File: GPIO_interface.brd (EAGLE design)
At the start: 38 x 34.5 mm, 33 parts

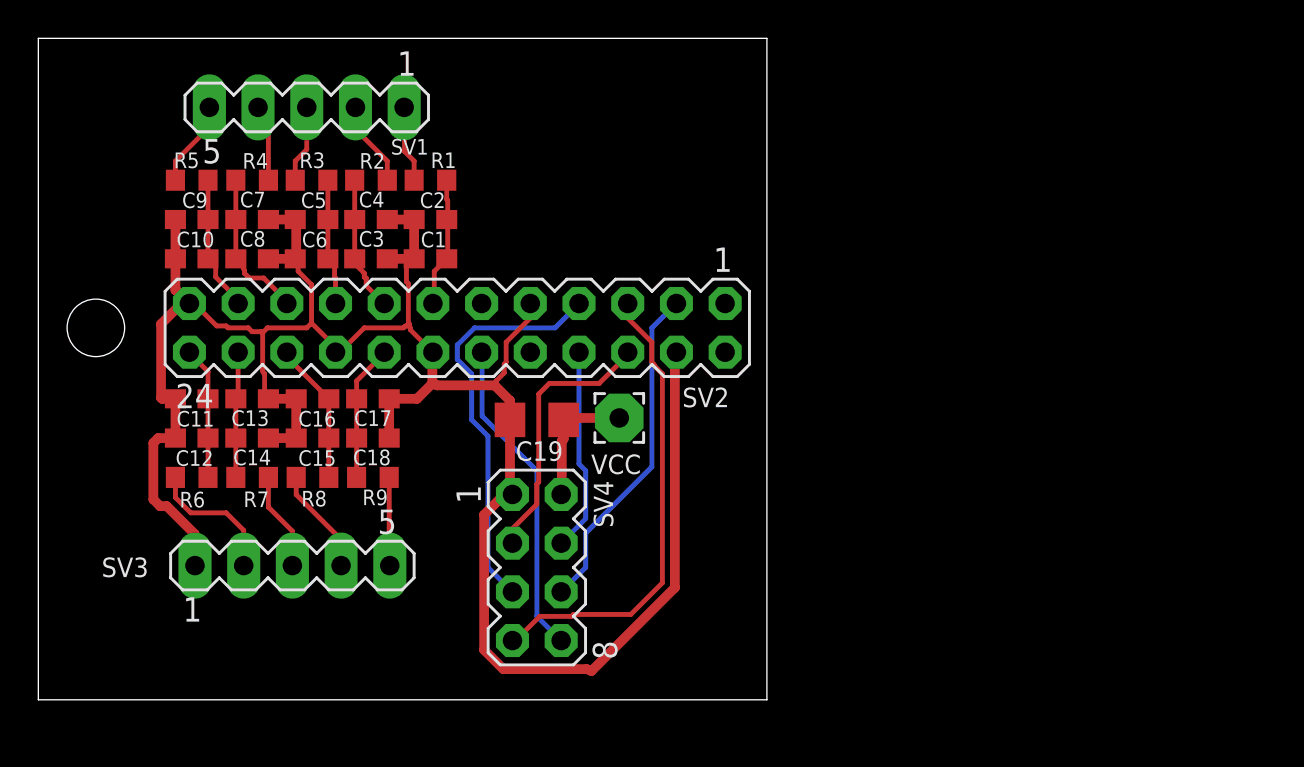
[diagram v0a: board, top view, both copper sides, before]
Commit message: wersja pod pcbs.io
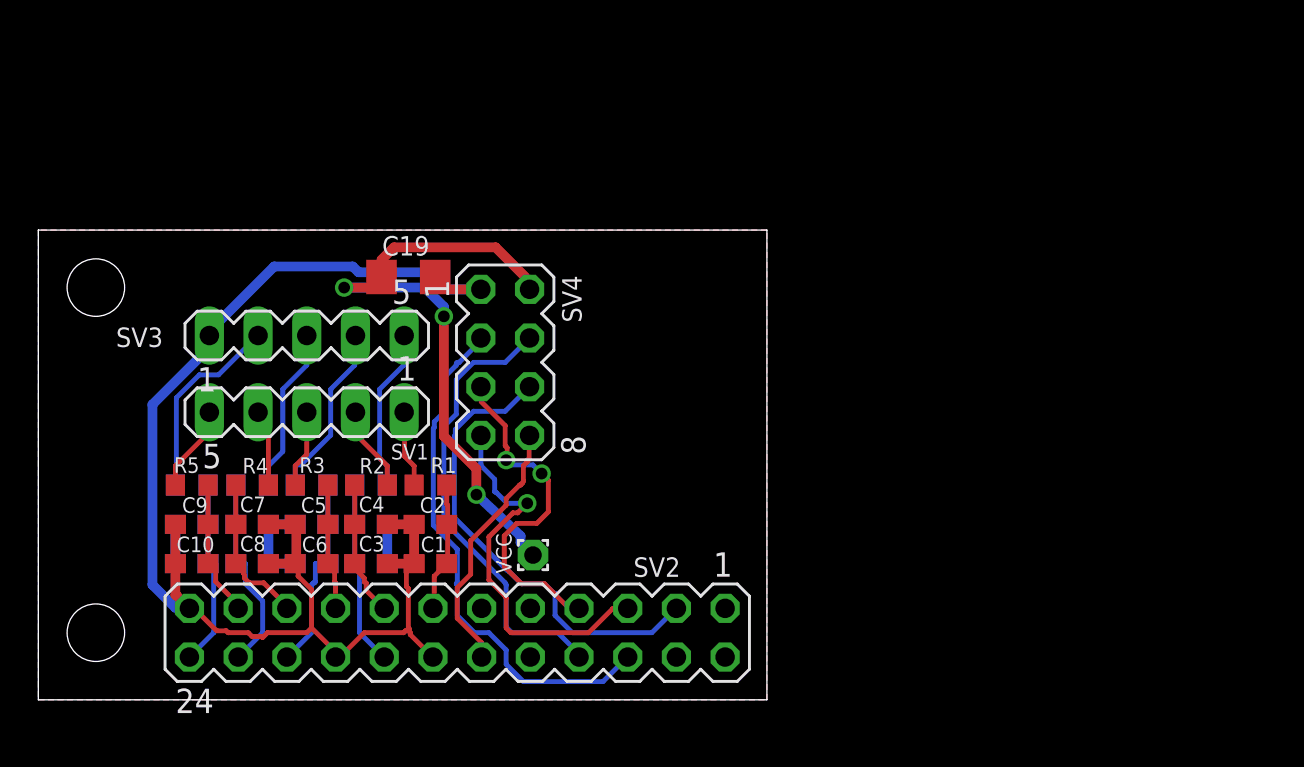
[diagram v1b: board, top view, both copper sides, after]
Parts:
- VCC: device wirepad:2,54/1,0 -> wirepad:1,6/0,9
- moved R1 15.9 mm to (20.4, 10.7)
- moved R2 15.9 mm to (17.4, 10.7)
- moved R3 15.9 mm to (14.2, 10.7)
- moved R4 15.9 mm to (11.2, 10.7)
- moved R5 15.9 mm to (8.00, 10.7)
- moved C1 15.9 mm to (20.4, 6.60)
- moved C10 15.9 mm to (8.00, 6.60)
- moved C2 15.9 mm to (20.4, 8.65)
- moved C3 15.9 mm to (17.4, 6.60)
- moved C4 15.9 mm to (17.4, 8.65)
- moved C5 15.9 mm to (14.2, 8.65)
- moved C6 15.9 mm to (14.2, 6.60)
- moved C7 15.9 mm to (11.2, 8.65)
- moved C8 15.9 mm to (11.2, 6.60)
- moved C9 15.9 mm to (8.00, 8.65)
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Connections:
- net GND: no longer SV2.4, SV2.9
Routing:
- net GND: track 117.4 -> 82.0 mm
- net VCC: track 6.94 -> 32.8 mm, vias 0 -> 3
- net CE: track 14.0 -> 27.4 mm
- net CSN: track 10.6 -> 23.8 mm
- net MOSI: track 17.5 -> 24.7 mm
- net MISO: track 24.4 -> 20.0 mm, vias 0 -> 1
- net IN9: track 4.61 -> 8.51 mm
- net IN8: track 5.57 -> 9.27 mm
- net OUT7: track 6.76 -> 10.4 mm
- net IN7: track 5.12 -> 8.63 mm
- net SCK: track 21.3 -> 17.9 mm, vias 0 -> 2
- net IN6: track 7.16 -> 10.2 mm
- net OUT6: track 6.93 -> 9.80 mm
- net IRQ: track 16.8 -> 13.9 mm
- net OUT8: track 7.44 -> 10.3 mm
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- added copper zone on layer 1, net GND
- added copper zone on layer 16, net GND
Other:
- board size 38 x 34.5 mm -> 38 x 24.5 mm

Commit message: add LDO, use whole RPI connector
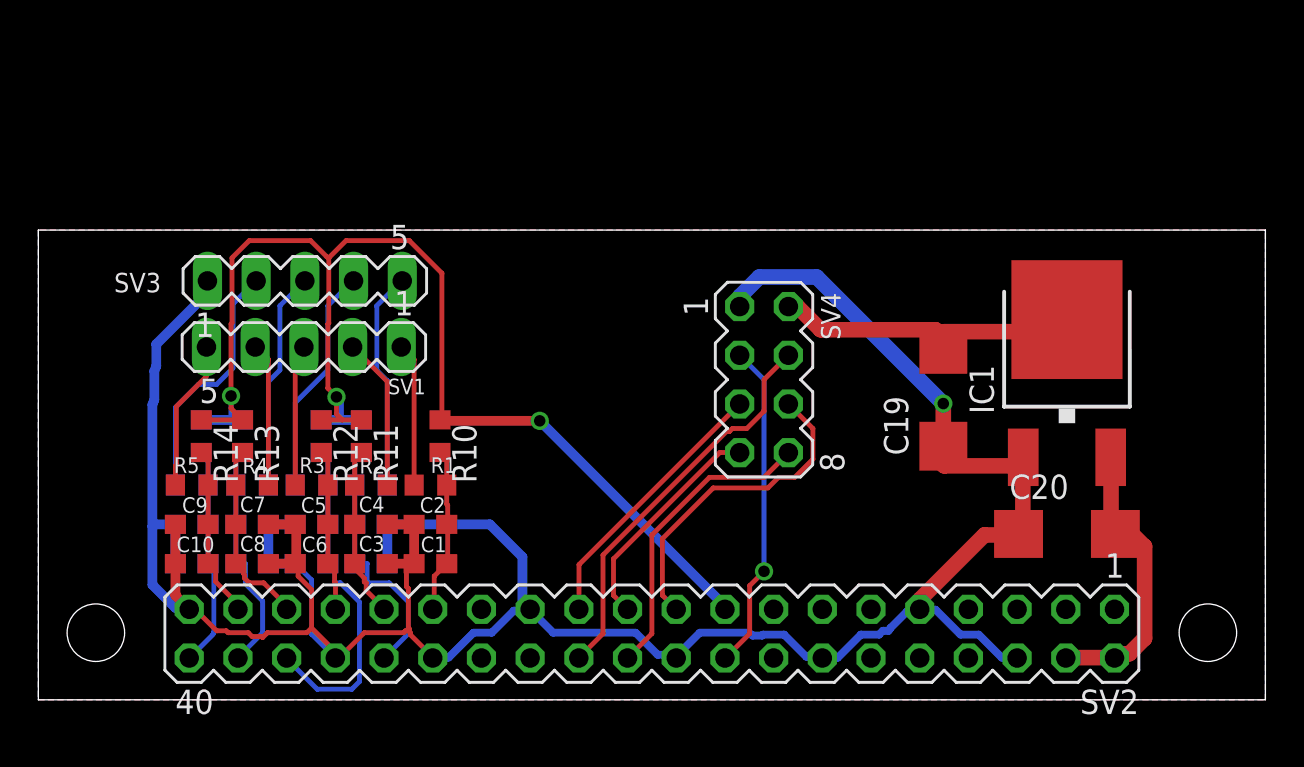
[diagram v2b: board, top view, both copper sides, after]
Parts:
- removed VCC: 3.3V, wirepad:1,6/0,9
- added C20: 10u, rcl:C/6032-28R
- added IC1: LD117ADT33TR, v-reg:DPACK
- added R10, R11, R12, R13, R14, R15, R16, R17, R18: 270, rcl:R0603
- C19: device rcl:C1206 -> rcl:C/6032-28R
- SV2: device con-lstb:MA12-2 -> con-lstb:MA20-2
- moved C19 28.6 mm to (47.2, 15.2), turned to 90 degrees
- moved SV4 13.5 mm to (37.9, 16.2)
- moved SV2 10.2 mm to (32.0, 2.95)
- moved SV1 3.40 mm to (13.8, 17.9)
- moved SV3 2.85 mm to (13.9, 21.4)
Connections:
- removed net CE: SV2.6, SV4.3
- new net N$1: C20.+, IC1.3, SV2.2, SV2.4
- new net N$2: C19.+, IC1.4, SV4.2
- new net RST: SV2.18, SV4.3
- net CSN: now also SV2.24; no longer SV2.8
- net GND: now also C19.-, C20.-, IC1.1, SV2.20, SV2.25, SV2.30, SV2.34, SV2.39, SV2.6, SV2.9; no longer C19.2, SV2.18, SV2.23
- net IRQ: now also SV2.22; no longer SV2.12
- net MISO: now also SV2.21; no longer SV2.5
- net MOSI: now also SV2.19; no longer SV2.3
- net OUT1: now also R10.2, SV2.29; no longer SV2.13
- net OUT2: now also R11.2, SV2.31; no longer SV2.15
- net OUT3: now also R12.2, SV2.33; no longer SV2.17
- net OUT4: now also R13.2, SV2.35; no longer SV2.19
- net OUT5: now also R14.2, SV2.37; no longer SV2.21
- net OUT6: now also R15.2, SV2.40; no longer SV2.24
- net OUT7: now also R16.2, SV2.38; no longer SV2.22
- net OUT8: now also R17.2, SV2.36; no longer SV2.20
- net OUT9: now also R18.2, SV2.32; no longer SV2.16
- net SCK: now also SV2.23; no longer SV2.7
- net VCC: now also R10.1, R11.1, R12.1, R13.1, R14.1, R15.1, R16.1, R17.1, R18.1, SV2.17; no longer C19.1, SV4.2, VCC.1
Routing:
- net GND: track 82.0 -> 152.8 mm, vias 0 -> 1
- net VCC: track 32.8 -> 69.8 mm
- net CE: track 27.4 -> 0.00 mm
- net N$2: track 0.00 -> 17.3 mm
- net RST: track 0.00 -> 17.2 mm, vias 0 -> 1
- net N$1: track 0.00 -> 15.2 mm
- net MISO: track 20.0 -> 11.8 mm, vias 1 -> 0
- net OUT8: track 10.3 -> 18.0 mm
- net MOSI: track 24.7 -> 17.0 mm
- net OUT9: track 9.76 -> 13.8 mm
- net SCK: track 17.9 -> 14.2 mm, vias 2 -> 0
- net IN4: track 4.05 -> 7.51 mm
- net IN2: track 4.49 -> 7.96 mm
- net IN1: track 4.03 -> 7.49 mm
- net IN5: track 4.54 -> 7.88 mm
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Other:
- board size 38 x 24.5 mm -> 64 x 24.5 mm

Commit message: cleanup names on pcb
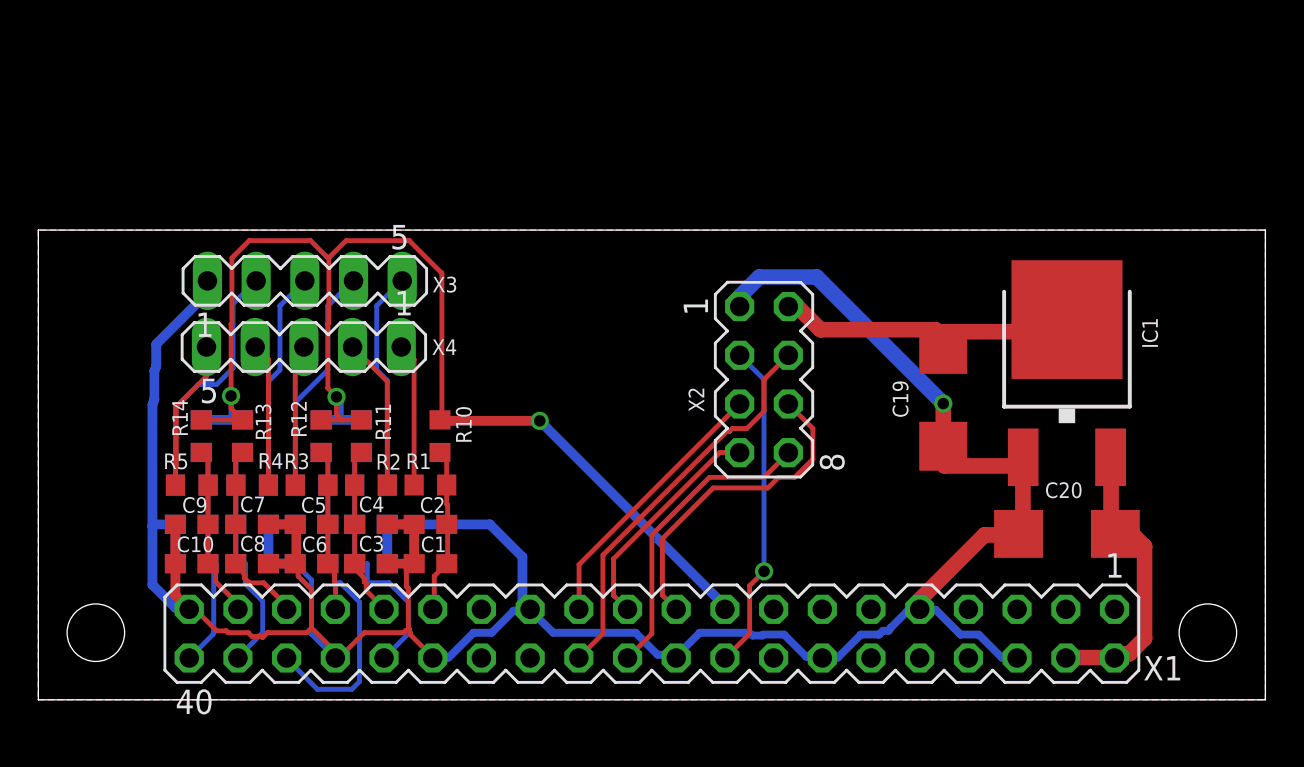
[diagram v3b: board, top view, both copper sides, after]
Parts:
- renumbered SV1 to X4, SV2 to X1, SV3 to X3, SV4 to X2
